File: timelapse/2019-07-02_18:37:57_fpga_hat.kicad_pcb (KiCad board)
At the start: 4 copper layers, 65 x 56.5 mm, 90 parts, among them J1 2x20, J2 AudioJack3, J3 Conn_02x06_Top_Bottom, J4 Conn_02x06_Top_Bottom, J5 Conn_02x06_Top_Bottom, J6 Conn_01x02, SW1 PTS815, SW2 PTS815, SW3 PTS815, SW4 PTS815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

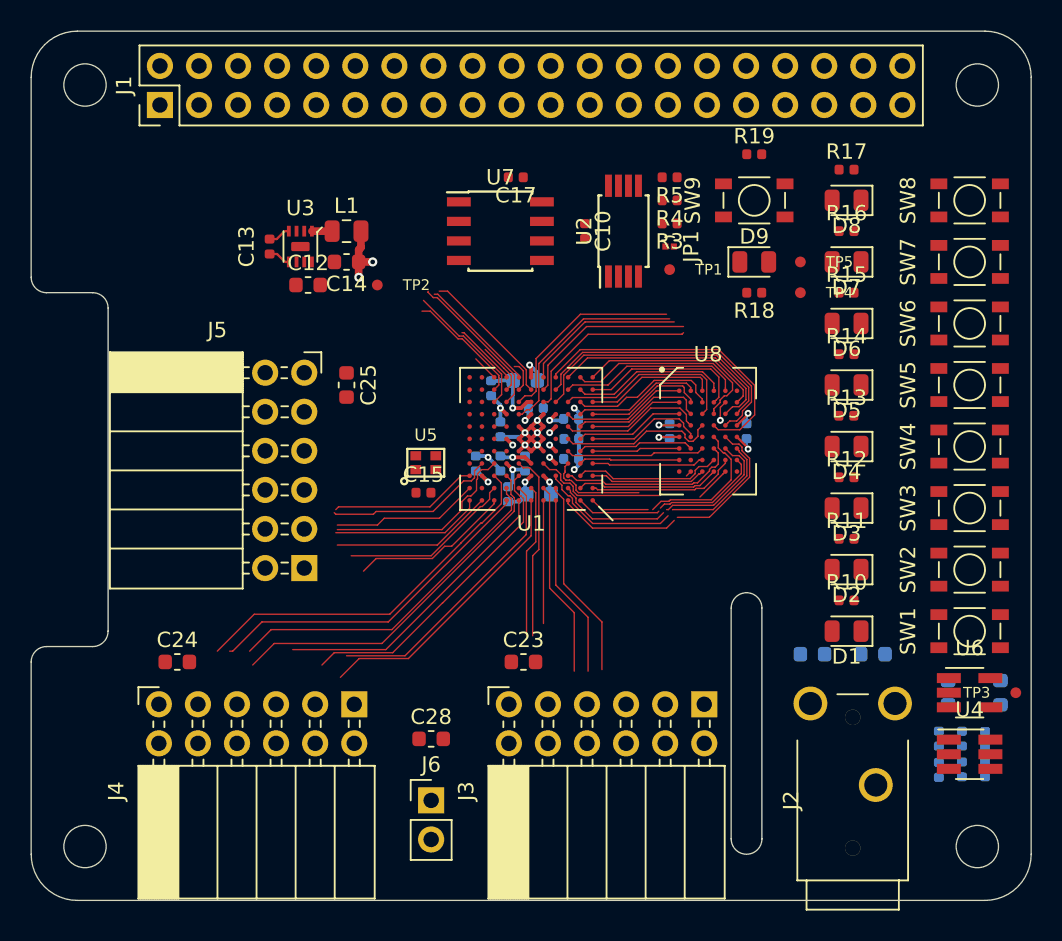
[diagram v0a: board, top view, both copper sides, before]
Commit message: SRAM escaped. Some work on FPGA power routing. Some SRAM pinswapping.
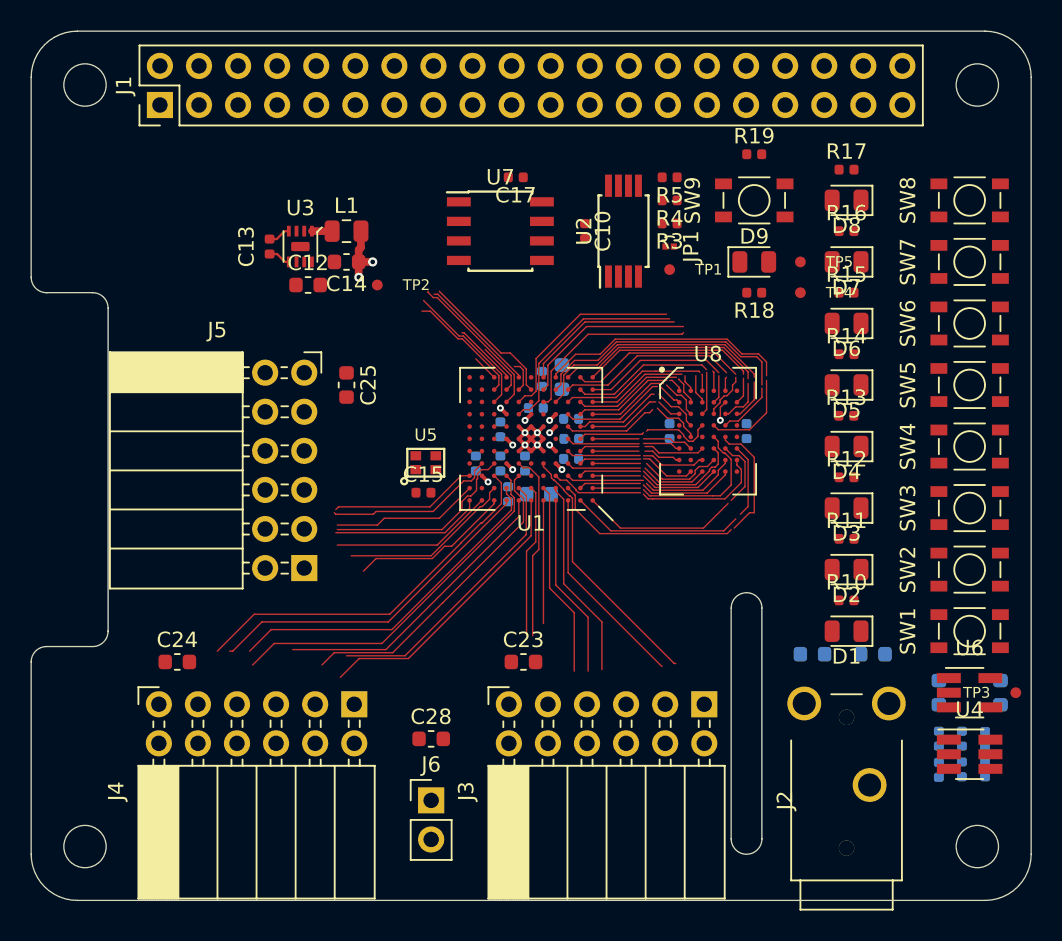
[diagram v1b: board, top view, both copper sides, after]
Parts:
- moved R2 3.36 mm to (133.2, 102.6), turned to 90 degrees
- moved C2 2.40 mm to (134.5, 102.5), turned to 90 degrees
- moved C16 0.60 mm to (159.0, 123.0)
- moved J2 0.40 mm to (153.0, 129.0)
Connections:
- U1 pad B1: /SRAM_~WE -> /SRAM_DQ0
- U1 pad B2: /SRAM_A10 -> /SRAM_DQ1
- U1 pad C1: /SRAM_A9 -> /SRAM_DQ5
- U1 pad C2: /SRAM_A13 -> /SRAM_DQ4
- U1 pad C3: /SRAM_A15 -> /SRAM_DQ3
- U1 pad C4: /SRAM_A11 -> /SRAM_DQ2
- U1 pad D1: /SRAM_A12 -> /SRAM_DQ7
- U1 pad D2: /SRAM_DQ15 -> /SRAM_DQ8
- U1 pad D3: /SRAM_A8 -> /SRAM_DQ9
- U1 pad E1: /SRAM_DQ14 -> /SRAM_DQ6
- U1 pad E2: /SRAM_DQ13 -> /SRAM_DQ10
- U1 pad E3: /SRAM_A14 -> /SRAM_A9
- U1 pad F1: /SRAM_DQ12 -> /SRAM_A0
- U1 pad F2: /SRAM_DQ9 -> /SRAM_DQ13
- U1 pad F3: /SRAM_A17 -> /SRAM_A8
- U1 pad F4: /SRAM_DQ6 -> /SRAM_DQ14
- U1 pad G1: /SRAM_DQ8 -> /SRAM_DQ11
- U1 pad G2: /SRAM_DQ10 -> /SRAM_DQ15
- U1 pad G3: /SRAM_DQ11 -> /SRAM_DQ12
- U1 pad H1: /SRAM_~UB -> /SRAM_A2
- U1 pad H2: /SRAM_~OE -> /SRAM_A3
- U1 pad H3: /SRAM_~LB -> /SRAM_A1
- U1 pad H7: /SRAM_DQ7 -> /SRAM_~LB
- U1 pad J1: /SRAM_A0 -> /SRAM_A4
- U1 pad J2: /SRAM_A3 -> /SRAM_A7
- U1 pad J3: /SRAM_A5 -> /SRAM_A11
- U1 pad J4: /SRAM_DQ2 -> /SRAM_A14
- U1 pad J5: /SRAM_DQ5 -> /SRAM_~WE
- U1 pad J7: /SRAM_DQ4 -> /SRAM_~UB
- U1 pad K1: /SRAM_A4 -> /SRAM_A5
- U1 pad K2: /SRAM_A1 -> /SRAM_A6
- U1 pad K3: /SRAM_A2 -> /SRAM_A13
- U1 pad K4: /SRAM_DQ3 -> /SRAM_A17
- U1 pad K5: /SRAM_A16 -> /SRAM_~OE
- U1 pad L1: /SRAM_DQ0 -> /SRAM_A10
- U1 pad L2: /SRAM_A6 -> /SRAM_A12
- U1 pad L3: /SRAM_DQ1 -> /SRAM_A15
- U1 pad L4: /SRAM_A7 -> /SRAM_A16
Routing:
- net GND: track 24.9 -> 10.4 mm, vias 11 -> 5
- net /SRAM_DQ5: track 20.5 -> 7.62 mm
- net /SRAM_A17: track 10.3 -> 21.8 mm
- net /SRAM_A14: track 9.03 -> 20.2 mm
- net /SRAM_DQ4: track 22.5 -> 11.9 mm
- net /SRAM_DQ3: track 18.5 -> 8.76 mm
- net /SRAM_DQ7: track 21.0 -> 11.6 mm
- net /SRAM_A15: track 11.7 -> 20.6 mm
- net /SRAM_DQ2: track 17.4 -> 8.65 mm
- net /SRAM_~WE: track 9.73 -> 18.4 mm
- net /SRAM_A12: track 7.30 -> 15.8 mm
- net /SRAM_DQ1: track 15.4 -> 7.02 mm
- net +3V3: track 10.9 -> 2.83 mm, vias 8 -> 5
- net /IO1_7: track 9.02 -> 16.7 mm
- net /SRAM_A13: track 9.63 -> 17.1 mm
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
